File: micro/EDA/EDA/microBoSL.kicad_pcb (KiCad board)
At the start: 4 copper layers, 40 x 13 mm, 49 parts, among them J1 Conn_01x04, J2 Conn_01x03, J3 Conn_01x04, J4 BATTERY CONN, J5 Conn_02x03_Odd_Even, J6 Conn_01x04, J7 MOTOR_OUT, J8 USB_B_Micro, Q1 DMP2165UW, SW1 RST_JMPR, SW2 AYZ0103AGRLC, U1 TPS709A33DBVT, U2 TPS709A33DBVT, U3 ATmega328P-MMH, U4 ZXBM5210-S, U5 74HC126PW-Q100, U6 MCP7940N-xSN, U7 FT232RQ, Y1 8MHz, Y2 32.768 kHz

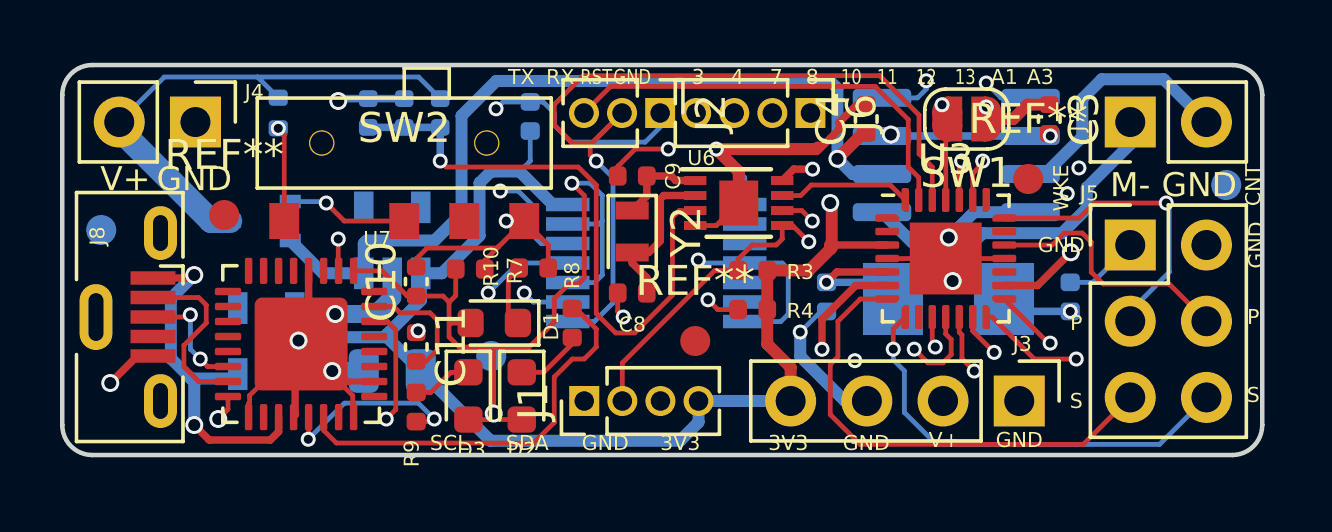
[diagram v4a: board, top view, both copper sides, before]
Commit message: added silkscreen to microbosl
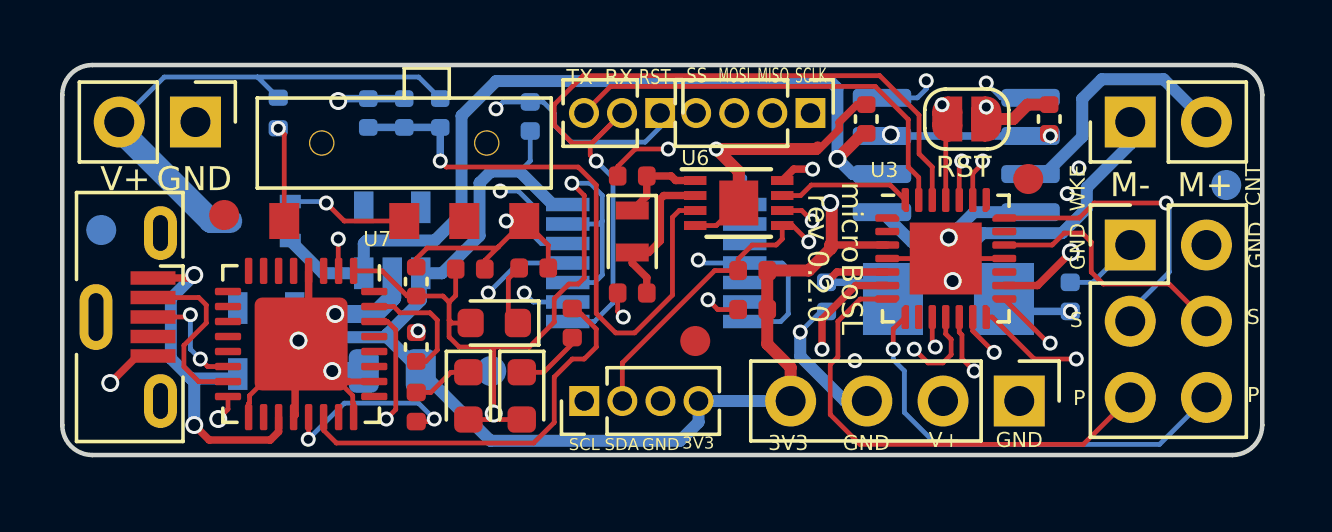
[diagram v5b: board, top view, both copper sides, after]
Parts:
- removed SW1: RST_JMPR, Jumper:SolderJumper-2_P1.3mm_Open_RoundedPad1.0x1.5mm
- added RST: RST_JMPR, Jumper:SolderJumper-2_P1.3mm_Open_RoundedPad1.0x1.5mm, F.Cu at (130.2, 103.8)
- moved REF** 0.50 mm to (114.3, 112.2)
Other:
- board text added: "M+"
- board text added: "MISO"
- board text added: "MOSI"
- board text added: "SCLK"
- board text added: "SS"
- board text added: "microBoSL rev 0.2.0"
- board text removed: "10"
- board text removed: "11"
- board text removed: "12"
- board text removed: "13"
- board text removed: "3"
- board text removed: "4"
- board text removed: "7"
- board text removed: "8"
- board text removed: "A1"
- board text removed: "A3"
- board text removed: "microBoSL rev 0.1.0"

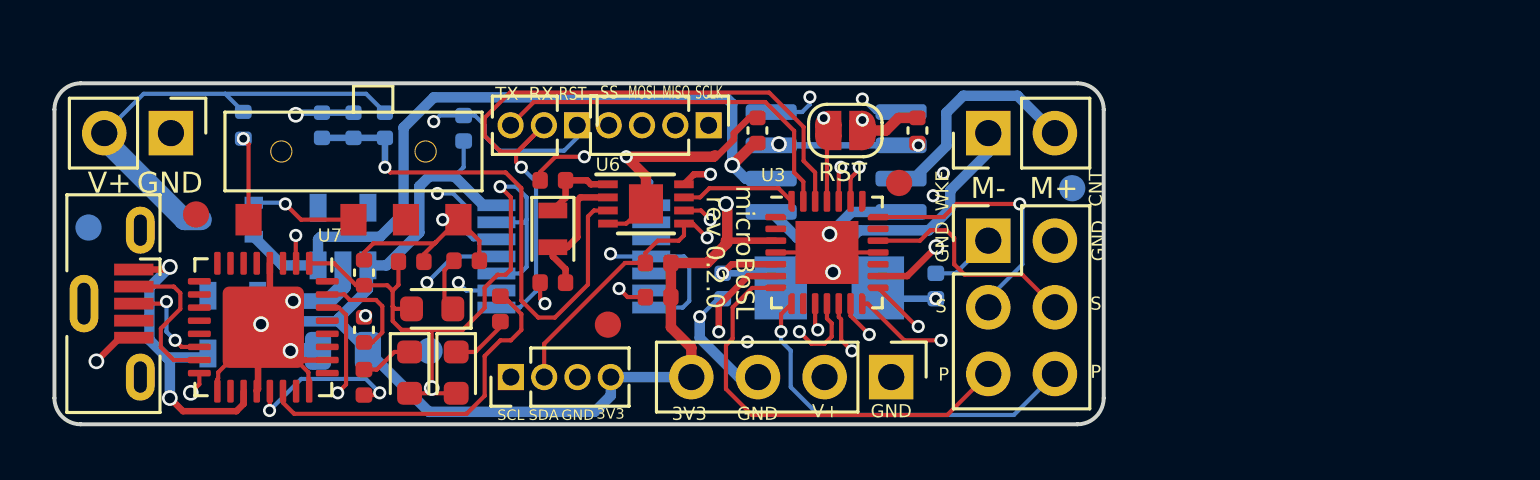
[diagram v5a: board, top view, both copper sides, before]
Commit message: added 3 motors to the microBoSL in schematic and PCB, traces and silkscreen still need optimising
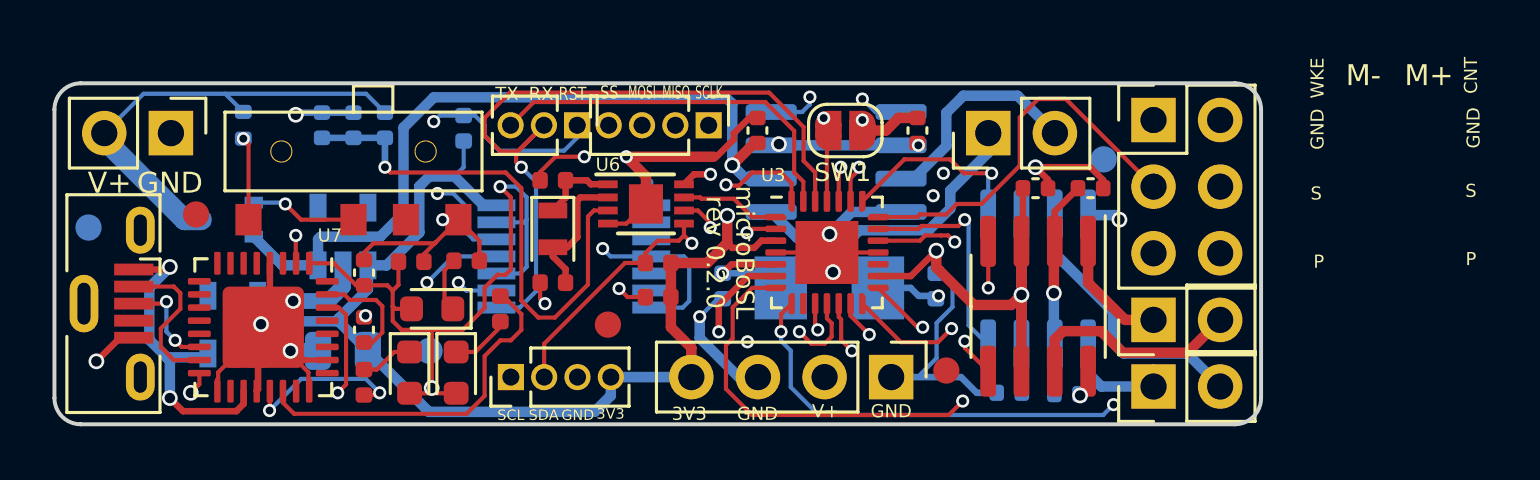
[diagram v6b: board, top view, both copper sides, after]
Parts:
- added C12: 100 nF, Capacitor_SMD:C_0402_1005Metric, F.Cu at (139.5, 106.0)
- added C13: 100 nF, Capacitor_SMD:C_0402_1005Metric, B.Cu at (136.4, 113.8)
- added C14: 100 nF, Capacitor_SMD:C_0402_1005Metric, B.Cu at (138.6, 113.8)
- added C2: 100 nF, Capacitor_SMD:C_0402_1005Metric, F.Cu at (137.4, 106.0)
- added J10: MOTOR_OUT, Connector_PinHeader_2.54mm:PinHeader_1x02_P2.54mm_Vertical, F.Cu at (141.9, 113.6)
- added J9: MOTOR_OUT, Connector_PinHeader_2.54mm:PinHeader_1x02_P2.54mm_Vertical, F.Cu at (141.9, 111.0)
- added U8: ZXBM5210-S, Package_SO:SOIC-8_3.9x4.9mm_P1.27mm, F.Cu at (137.5, 110.5)
- added U9: ZXBM5210-S, Package_SO:SOIC-8_3.9x4.9mm_P1.27mm, B.Cu at (137.5, 109.5)
- moved J5 7.80 mm to (141.9, 103.4)
- moved REF** 7.37 mm to (134.0, 113.0)
- moved REF** 1.63 mm to (140.0, 104.9)
- renumbered RST to SW1
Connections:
- net MFWD renamed MFWD_A
- net MREV renamed MREV_A
- U3 pad 1: D3 -> RTC_I
- U3 pad 2: D4 -> MREV_B
- U3 pad 20: A1 -> MFWD_C
- U3 pad 22: A3 -> MREV_C
- U3 pad 28: RTC_I -> MFWD_B
- U6 pad 9: GND -> (no net)
- U7 pad 33: GND -> (no net)
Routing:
- net MFWD_B: track 0.00 -> 33.4 mm, vias 0 -> 2
- net MREV_B: track 0.00 -> 27.3 mm, vias 0 -> 2
- net VBAT: track 43.3 -> 65.4 mm, vias 1 -> 2
- net V_3.3: track 60.9 -> 79.9 mm, vias 5 -> 6
- net GND: track 70.9 -> 85.3 mm, vias 14 -> 17
- net Net-(J10-Pad2): track 0.00 -> 10.6 mm
- net Hall_CNT_P: track 14.7 -> 25.2 mm, vias 1 -> 2
- net MFWD_C: track 0.00 -> 8.59 mm, vias 0 -> 1
- net Net-(J9-Pad2): track 0.00 -> 8.50 mm
- net Hall_WKE_P: track 16.2 -> 24.4 mm, vias 0 -> 1
- net MREV_C: track 0.00 -> 7.46 mm, vias 0 -> 1
- net Hall_CNT_S: track 8.71 -> 14.1 mm, vias 0 -> 1
- net Hall_WKE_S: track 10.1 -> 14.8 mm, vias 1 -> 0
- net Net-(J9-Pad1): track 0.00 -> 4.66 mm
- net Net-(J10-Pad1): track 0.00 -> 4.52 mm
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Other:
- board size 40 x 13 mm -> 46 x 13 mm

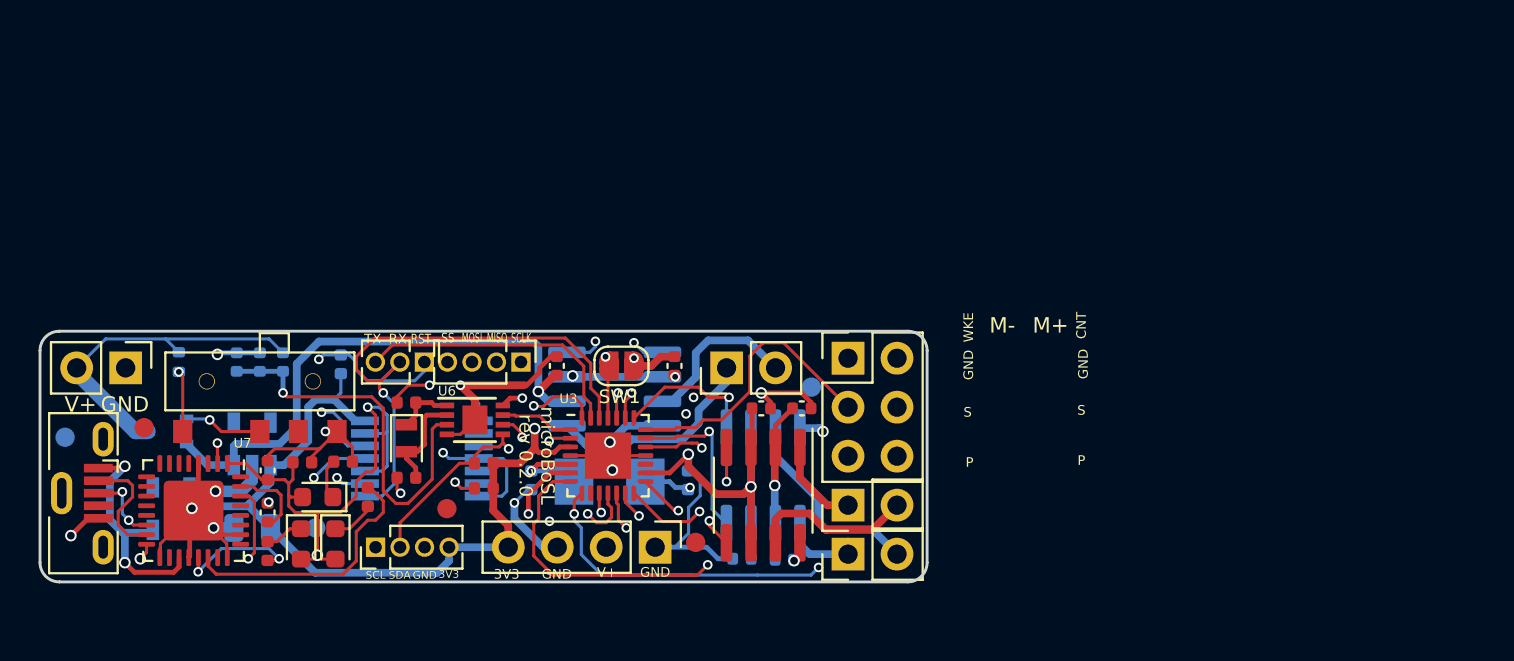
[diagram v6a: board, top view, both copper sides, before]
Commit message: routed pcb with 4 hall effect sensors, TODO silkscreen
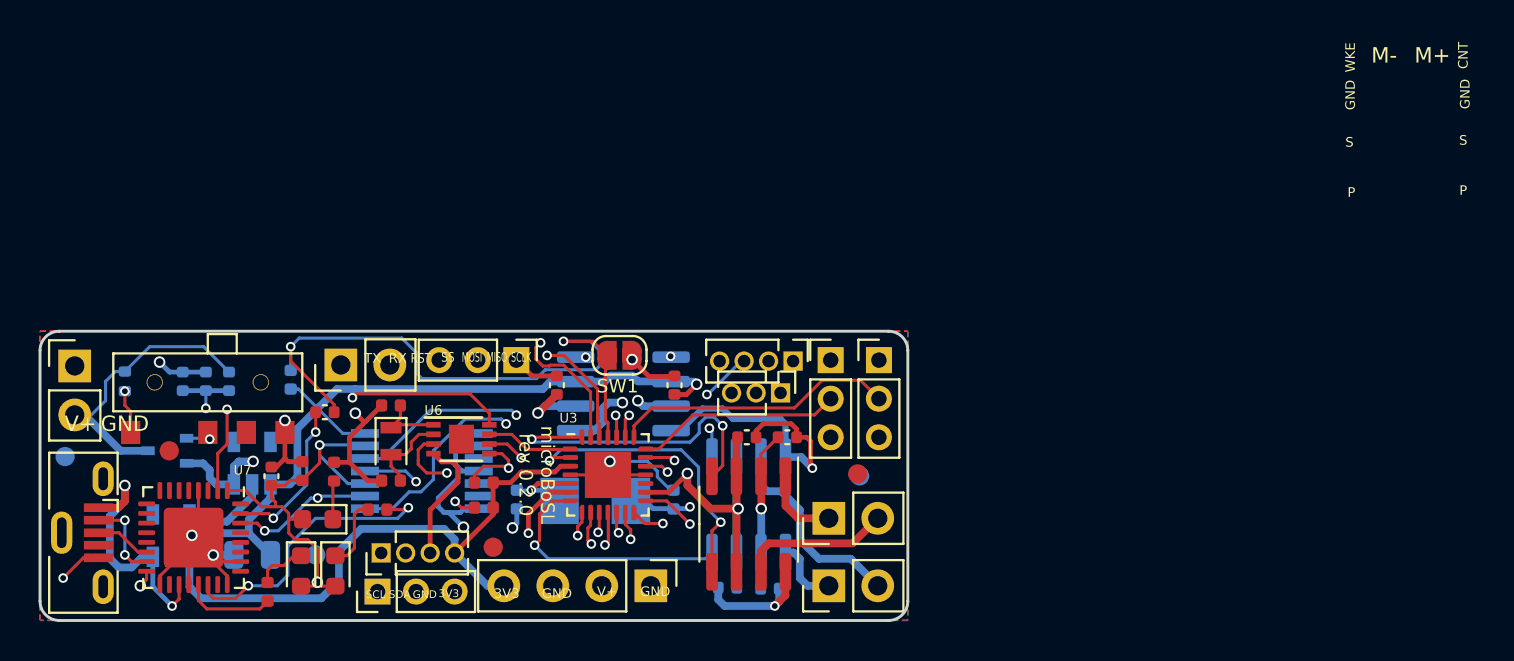
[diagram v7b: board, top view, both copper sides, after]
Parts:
- removed the REF** at (101.3, 107.5)
- removed the REF** at (114.3, 112.2)
- removed the REF** at (105.4, 107.0)
- added J11: Conn_01x03, Connector_PinHeader_2.00mm:PinHeader_1x03_P2.00mm_Vertical, F.Cu at (124.7, 103.5)
- added J12: Conn_01x03, Connector_PinHeader_2.00mm:PinHeader_1x03_P2.00mm_Vertical, F.Cu at (141.0, 103.5)
- added J13: Conn_01x03, Connector_PinHeader_2.00mm:PinHeader_1x03_P2.00mm_Vertical, F.Cu at (143.5, 103.5)
- added REF**: Fiducial_1mm_Mask2mm, Fiducial:Fiducial_1mm_Mask2mm, B.Cu at (101.3, 108.5)
- added REF**: Fiducial_1mm_Mask2mm, Fiducial:Fiducial_1mm_Mask2mm, B.Cu at (114.3, 113.6)
- added REF**: Fiducial_1mm_Mask2mm, Fiducial:Fiducial_1mm_Mask2mm, F.Cu at (106.7, 108.2)
- J5: value Conn_02x03_Odd_Even -> Conn_01x03; footprint Connector_PinHeader_2.54mm:PinHeader_2x03_P2.54mm_Vertical -> Connector_PinHeader_2.00mm:PinHeader_1x03_P2.00mm_Vertical
- moved J5 27.2 mm to (117.5, 115.5), turned to 90 degrees
- moved REF** 21.4 mm to (142.4, 109.4)
- moved J7 20.0 mm to (115.6, 103.8)
- moved J2 18.5 mm to (138.4, 105.2)
- moved J6 14.1 mm to (139.1, 103.5)
- moved REF** 10.5 mm to (123.5, 113.2)
- moved C11 5.99 mm to (114.8, 106.2), turned to 180 degrees
- moved REF** 5.24 mm to (142.5, 109.5)
- moved C7 2.97 mm to (108.6, 104.6)
- moved R1 2.97 mm to (104.4, 104.6)
- moved R5 2.97 mm to (109.8, 104.6)
- moved R6 2.97 mm to (107.4, 104.6)
- moved R2 2.72 mm to (113.0, 104.5)
- moved SW2 2.70 mm to (108.7, 104.7)
- moved J4 2.64 mm to (101.8, 103.8), turned to 0 degrees
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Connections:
- J5 pad 2: GND -> Hall_WKE_S
- J5 pad 3: Hall_WKE_S -> Hall_P
- U3 pad 19: Hall_CNT_S -> Hall_WKE_S
- U3 pad 20: MFWD_C -> Hall_MA_S
- U3 pad 21: Hall_WKE_S -> Hall_MB_S
- U3 pad 22: MREV_C -> Hall_MC_S
- U3 pad 7: Hall_WKE_P -> MFWD_C
- U3 pad 8: Hall_CNT_P -> MREV_C
- U3 pad 9: D7 -> Hall_P
- U7 pad 33: (no net) -> GND
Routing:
- net Hall_P: track 0.00 -> 42.6 mm, vias 0 -> 1
- net GND: track 85.3 -> 117.8 mm, vias 17 -> 12
- net V_3.3: track 79.9 -> 105.1 mm, vias 6 -> 4
- net Hall_CNT_P: track 25.2 -> 0.00 mm, vias 2 -> 0
- net Hall_WKE_P: track 24.4 -> 0.00 mm, vias 1 -> 0
- net MFWD_B: track 33.4 -> 16.5 mm
- net TLL_RST: track 29.3 -> 45.8 mm, vias 3 -> 2
- net Hall_MA_S: track 0.00 -> 15.5 mm, vias 0 -> 1
- net Hall_MC_S: track 0.00 -> 14.7 mm
- net Hall_CNT_S: track 14.1 -> 0.00 mm, vias 1 -> 0
- net TLL_TX: track 22.2 -> 34.2 mm, vias 1 -> 2
- net MREV_B: track 27.3 -> 15.6 mm
- net Hall_MB_S: track 0.00 -> 10.7 mm
- net Hall_WKE_S: track 14.8 -> 24.9 mm, vias 0 -> 1
- net MREV_C: track 7.46 -> 16.6 mm, vias 1 -> 2
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- added copper zone on B.Cu, net GND
- added copper zone on F.Cu, net GND
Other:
- board size 46 x 13 mm -> 45 x 15 mm

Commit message: micro traces optimised and silkscreened  TODO: panelisation
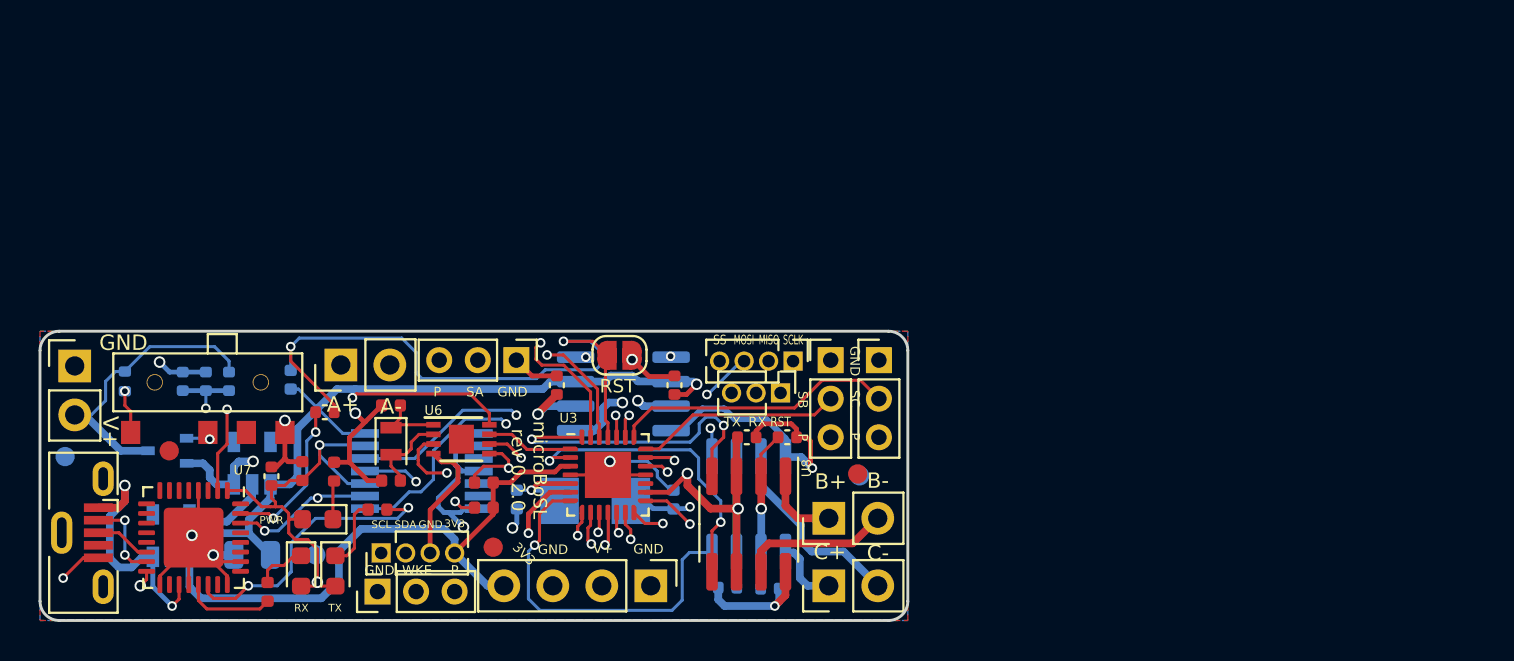
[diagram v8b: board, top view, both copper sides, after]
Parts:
- renumbered SW1 to RST
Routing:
- net MFWD_C: track 13.2 -> 18.8 mm
- net Hall_WKE_S: track 24.9 -> 21.6 mm
- net Hall_P: track 42.6 -> 43.5 mm
- net MFWD_A: track 12.1 -> 12.7 mm
- net GND: track 117.8 -> 117.3 mm
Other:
- board text added: "A+"
- board text added: "A-"
- board text added: "B+"
- board text added: "B-"
- board text added: "C+"
- board text added: "C-"
- board text added: "PWR"
- board text added: "SA"
- board text added: "SB"
- board text added: "SC"
- board text removed: "CNT"
- board text removed: "M+"
- board text removed: "M-"
- board text removed: "S"
